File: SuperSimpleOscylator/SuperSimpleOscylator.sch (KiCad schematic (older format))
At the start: 5 parts

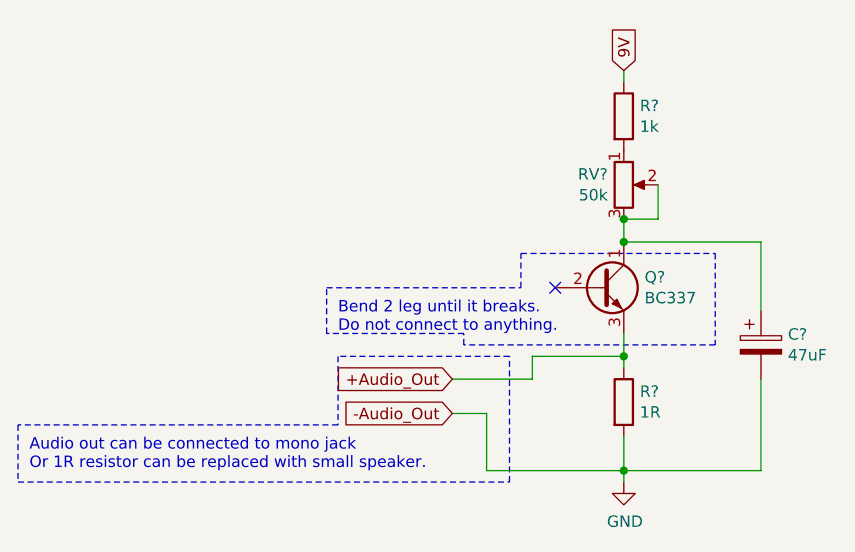
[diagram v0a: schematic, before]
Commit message: SCHEMATIC: updated names of components
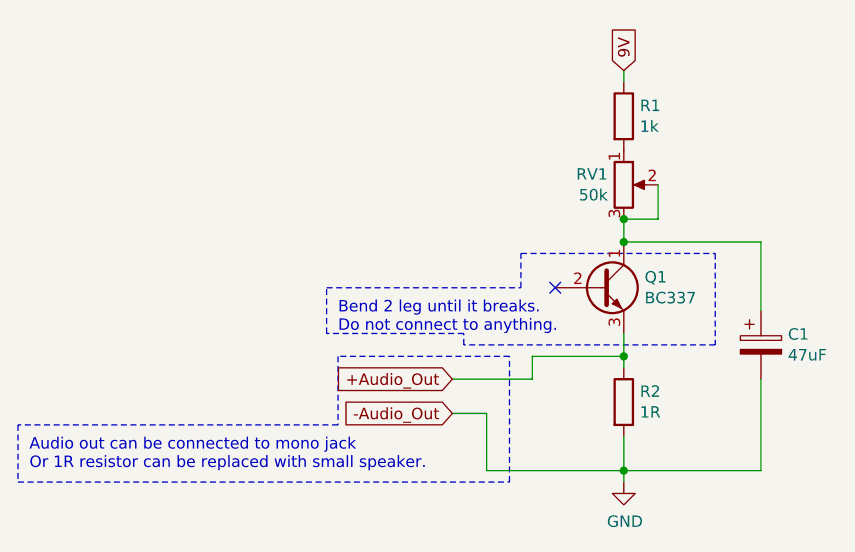
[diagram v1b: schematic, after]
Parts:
- gave numbers to parts that had none: 5
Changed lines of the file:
@@
 $EndDescr
 $Comp
-L Transistor_BJT:BC337 Q?
+L Transistor_BJT:BC337 Q1
 U 1 1 607DE5D3
 P 6300 3750
-F 0 "Q?" H 6491 3796 50  0000 L CNN
+F 0 "Q1" H 6491 3796 50  0000 L CNN
 F 1 "BC337" H 6491 3705 50  0000 L CNN
 F 2 "Package_TO_SOT_THT:TO-92_Inline" H 6500 3675 50  0001 L CIN
@@
 $EndComp
 $Comp
-L Device:R R?
+L Device:R R1
 U 1 1 607DEB60
 P 6400 3000
-F 0 "R?" H 6470 3046 50  0000 L CNN
+F 0 "R1" H 6470 3046 50  0000 L CNN
 F 1 "1k" H 6470 2955 50  0000 L CNN
 F 2 "" V 6330 3000 50  0001 C CNN
@@
 $EndComp
 $Comp
-L Device:R_POT RV?
+L Device:R_POT RV1
 U 1 1 607DF31D
 P 6400 3300
-F 0 "RV?" H 6330 3346 50  0000 R CNN
+F 0 "RV1" H 6330 3346 50  0000 R CNN
 F 1 "50k" H 6330 3255 50  0000 R CNN
 F 2 "" H 6400 3300 50  0001 C CNN
@@
 $EndComp
 $Comp
-L Device:R R?
+L Device:R R2
 U 1 1 607DF9A8
 P 6400 4250
-F 0 "R?" H 6470 4296 50  0000 L CNN
+F 0 "R2" H 6470 4296 50  0000 L CNN
 F 1 "1R" H 6470 4205 50  0000 L CNN
 F 2 "" V 6330 4250 50  0001 C CNN
@@
 $EndComp
 $Comp
-L Device:CP C?
+L Device:CP C1
 U 1 1 607DFEC9
 P 7000 4000
-F 0 "C?" H 7118 4046 50  0000 L CNN
+F 0 "C1" H 7118 4046 50  0000 L CNN
 F 1 "47uF" H 7118 3955 50  0000 L CNN
 F 2 "" H 7038 3850 50  0001 C CNN
@@
 $EndComp
 $Comp
-L power:GND #PWR?
+L power:GND #PWR0101
 U 1 1 607E09C0
 P 6400 4600
-F 0 "#PWR?" H 6400 4350 50  0001 C CNN
+F 0 "#PWR0101" H 6400 4350 50  0001 C CNN
 F 1 "GND" H 6405 4427 50  0000 C CNN
 F 2 "" H 6400 4600 50  0001 C CNN
